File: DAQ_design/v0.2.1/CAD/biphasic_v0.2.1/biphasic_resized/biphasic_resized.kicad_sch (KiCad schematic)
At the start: 21 parts, among them Q1 BC549, Q2 IRF9540N, Q3 IRF540N, Q4 BC549, Q5 IRF540N, Q6 IRF9540N

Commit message: begin redraw
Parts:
- added J1: Conn_01x03_Pin, Connector_PinHeader_2.54mm:PinHeader_1x03_P2.54mm_Vertical, symbol Connector:Conn_01x03_Pin
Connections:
- net at Arduino1.5 (D2): now also J1.1 (Pin_1)
- net at Arduino1.6 (D3): now also J1.2 (Pin_2)
- net at Arduino1.7 (D4): now also J1.3 (Pin_3)
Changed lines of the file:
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@@
+    (stroke (width 0) (type default))
+  )
+  (wire (pts (xy 97.79 114.3) (xy 124.46 114.3))
     (stroke (width 0) (type default))
   )
@@
     (stroke (width 0) (type default))
   )
+  (wire (pts (xy 97.79 109.22) (xy 124.46 109.22))
+    (stroke (width 0) (type default))
+  )
   (wire (pts (xy 182.88 120.65) (xy 182.88 124.46))
     (stroke (width 0) (type default))
@@
   )
   (wire (pts (xy 177.8 113.03) (xy 177.8 104.14))
+    (stroke (width 0) (type default))
+  )
+  (wire (pts (xy 97.79 111.76) (xy 124.46 111.76))
     (stroke (width 0) (type default))
   )
@@
         )
       )
+    )
+  )
+  (symbol (lib_id "Connector:Conn_01x03_Pin") (at 92.71 111.76 0) (unit 1)
+    (in_bom yes) (on_board yes) (dnp no) (fields_autoplaced)
+    (property "Reference" "J1" (at 93.345 104.14 0)
+      (effects (font (size 1.27 1.27)))
+    )
+    (property "Value" "Conn_01x03_Pin" (at 93.345 106.68 0)
+      (effects (font (size 1.27 1.27)))
+    )
+    (property "Footprint" "Connector_PinHeader_2.54mm:PinHeader_1x03_P2.54mm_Vertical" (at 92.71 111.76 0)
+      (effects (font (size 1.27 1.27)) hide)
+    )
+    (property "Datasheet" "~" (at 92.71 111.76 0)
+      (effects (font (size 1.27 1.27)) hide)
+    )
+    (pin "3")
+    (pin "1")
+    (pin "2")
+    (instances
+      (project "biphasic_resized"
+        (path "/52f50ad4-ebe6-41ec-9989-47b12e2d2ded"
+          (reference "J1") (unit 1)
+        )
+      )

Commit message: sd card
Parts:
- added D5, D6: LED, symbol Device:LED
- added J2: Micro_SD_Card, symbol Connector:Micro_SD_Card
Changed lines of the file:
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@@
+    )
+  )
+  (symbol (lib_id "Device:LED") (at 43.18 105.41 0) (unit 1)
+    (in_bom yes) (on_board yes) (dnp no) (fields_autoplaced)
+    (property "Reference" "D6" (at 41.5925 99.06 0)
+      (effects (font (size 1.27 1.27)))
+    )
+    (property "Value" "LED" (at 41.5925 101.6 0)
+      (effects (font (size 1.27 1.27)))
+    )
+    (property "Footprint" "" (at 43.18 105.41 0)
+      (effects (font (size 1.27 1.27)) hide)
+    )
+    (property "Datasheet" "~" (at 43.18 105.41 0)
+      (effects (font (size 1.27 1.27)) hide)
+    )
+    (pin "2")
+    (pin "1")
+    (instances
+      (project "biphasic_resized"
+        (path "/52f50ad4-ebe6-41ec-9989-47b12e2d2ded"
+          (reference "D6") (unit 1)
+        )
+      )
     )
   )
@@
         (path "/52f50ad4-ebe6-41ec-9989-47b12e2d2ded"
           (reference "#PWR013") (unit 1)
+        )
+      )
+    )
+  )
+  (symbol (lib_id "Connector:Micro_SD_Card") (at 54.61 52.07 0) (unit 1)
+    (in_bom yes) (on_board yes) (dnp no) (fields_autoplaced)
+    (property "Reference" "J2" (at 55.245 33.02 0)
+      (effects (font (size 1.27 1.27)))
+    )
+    (property "Value" "Micro_SD_Card" (at 55.245 35.56 0)
+      (effects (font (size 1.27 1.27)))
+    )
+    (property "Footprint" "" (at 83.82 44.45 0)
+      (effects (font (size 1.27 1.27)) hide)
+    )
+    (property "Datasheet" "http://katalog.we-online.de/em/datasheet/693072010801.pdf" (at 54.61 52.07 0)
+      (effects (font (size 1.27 1.27)) hide)
+    )
+    (pin "2")
+    (pin "5")
+    (pin "3")
+    (pin "4")
+    (pin "9")
+    (pin "8")
+    (pin "1")
+    (pin "7")
+    (pin "6")
+    (instances
+      (project "biphasic_resized"
+        (path "/52f50ad4-ebe6-41ec-9989-47b12e2d2ded"
+          (reference "J2") (unit 1)
         )
       )
@@
         )
       )
+    )
+  )
+  (symbol (lib_id "Device:LED") (at 43.18 96.52 0) (unit 1)
+    (in_bom yes) (on_board yes) (dnp no) (fields_autoplaced)
+    (property "Reference" "D5" (at 41.5925 90.17 0)
+      (effects (font (size 1.27 1.27)))
+    )
+    (property "Value" "LED" (at 41.5925 92.71 0)
+      (effects (font (size 1.27 1.27)))
+    )
+    (property "Footprint" "" (at 43.18 96.52 0)
+      (effects (font (size 1.27 1.27)) hide)
+    )
+    (property "Datasheet" "~" (at 43.18 96.52 0)
+      (effects (font (size 1.27 1.27)) hide)
+    )
+    (pin "1")
+    (pin "2")
+    (instances
+      (project "biphasic_resized"
+        (path "/52f50ad4-ebe6-41ec-9989-47b12e2d2ded"
+          (reference "D5") (unit 1)
+        )
+      )

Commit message: sync
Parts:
- removed J1: Conn_01x03_Pin, Connector_PinHeader_2.54mm:PinHeader_1x03_P2.54mm_Vertical, symbol Connector:Conn_01x03_Pin
- removed J2: Micro_SD_Card, symbol Connector:Micro_SD_Card
- added A1: SD_Card_Module, Charleslabs_Parts:SD_Card_Module, symbol CharlesLabs:SD_Card_Module
- added R1, R9: R, symbol Device:R
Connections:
- net GND: now also A1.6 (GND), R1.1, R9.1
- net at D6.1 (K): now also R9.2
- net LEDACT: now reaches D6.2 (A)
- net LEDACT: now also Arduino1.6 (D3)
- net SDCS: now reaches Arduino1.13 (D10)
- net SDCS: now also A1.2 (CS)
- net SDSI: now reaches Arduino1.14 (MOSI)
- net SDSI: now also A1.3 (MOSI)
- net SDSO: now reaches Arduino1.15 (MISO)
- net SDSO: now also A1.5 (MISO)
- net SDCLK: now reaches Arduino1.16 (SCK)
- net SDCLK: now also A1.4 (CLK)
- net 3V3: now reaches Arduino1.17 (3V3)
- net 3V3: now also A1.1 (3V3)
- net LEDPOW: now reaches Arduino1.5 (D2)
- net LEDPOW: now also D5.2 (A)
- net at D5.1 (K): now also R1.2
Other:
- moved on the sheet: BiPhasic_out1, D5, D6

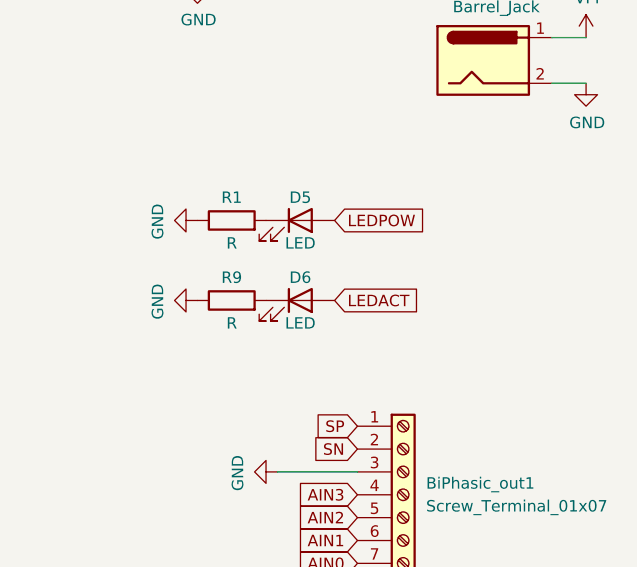
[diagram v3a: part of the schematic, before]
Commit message: dip surfboard
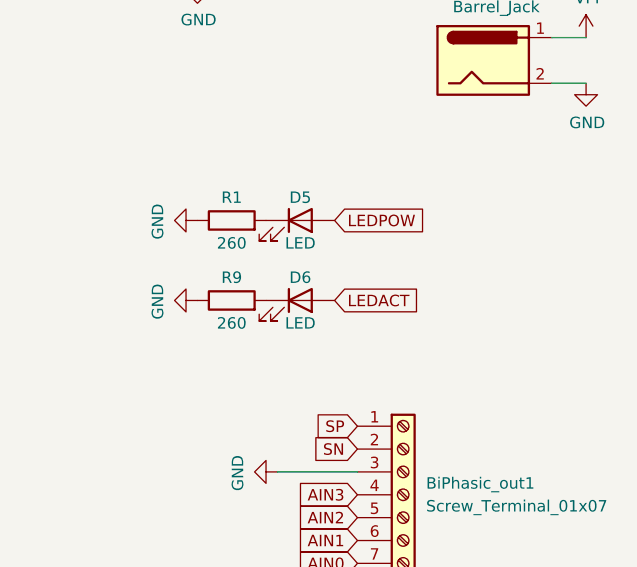
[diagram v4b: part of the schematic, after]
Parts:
- R1, R9: value R -> 260

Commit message: more tests
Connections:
- net AIN1 is gone; now on net AIN0: ADC1.8 (AIN1), BiPhasic_out1.6 (Pin_6), D2.1 (K)
- net AIN2 is gone; now on net AIN0: ADC1.9 (AIN2), BiPhasic_out1.5 (Pin_5), D3.1 (K)
- net AIN3 is gone; now on net AIN0: ADC1.10 (AIN3), BiPhasic_out1.4 (Pin_4), D4.1 (K)
- net SCL: now reaches ADC1.3 (SCL), Arduino1.24 (SCL/A5), R7.2
- net SDA: now reaches ADC1.4 (SDA), Arduino1.23 (SDA/A4), R8.2
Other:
- moved on the sheet: ADC1, BiPhasic_out1
